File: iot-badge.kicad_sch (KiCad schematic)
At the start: 50 parts, among them J1 USB_C_Receptacle_USB2.0, J2 Wire ANT, Q1 BC847, Q2 BC847, SW1 SW_Push, SW2 SW_Push, SW3 SW_Push, SW4 SW_Push, SW5 SW_Push, SW6 SW_Push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

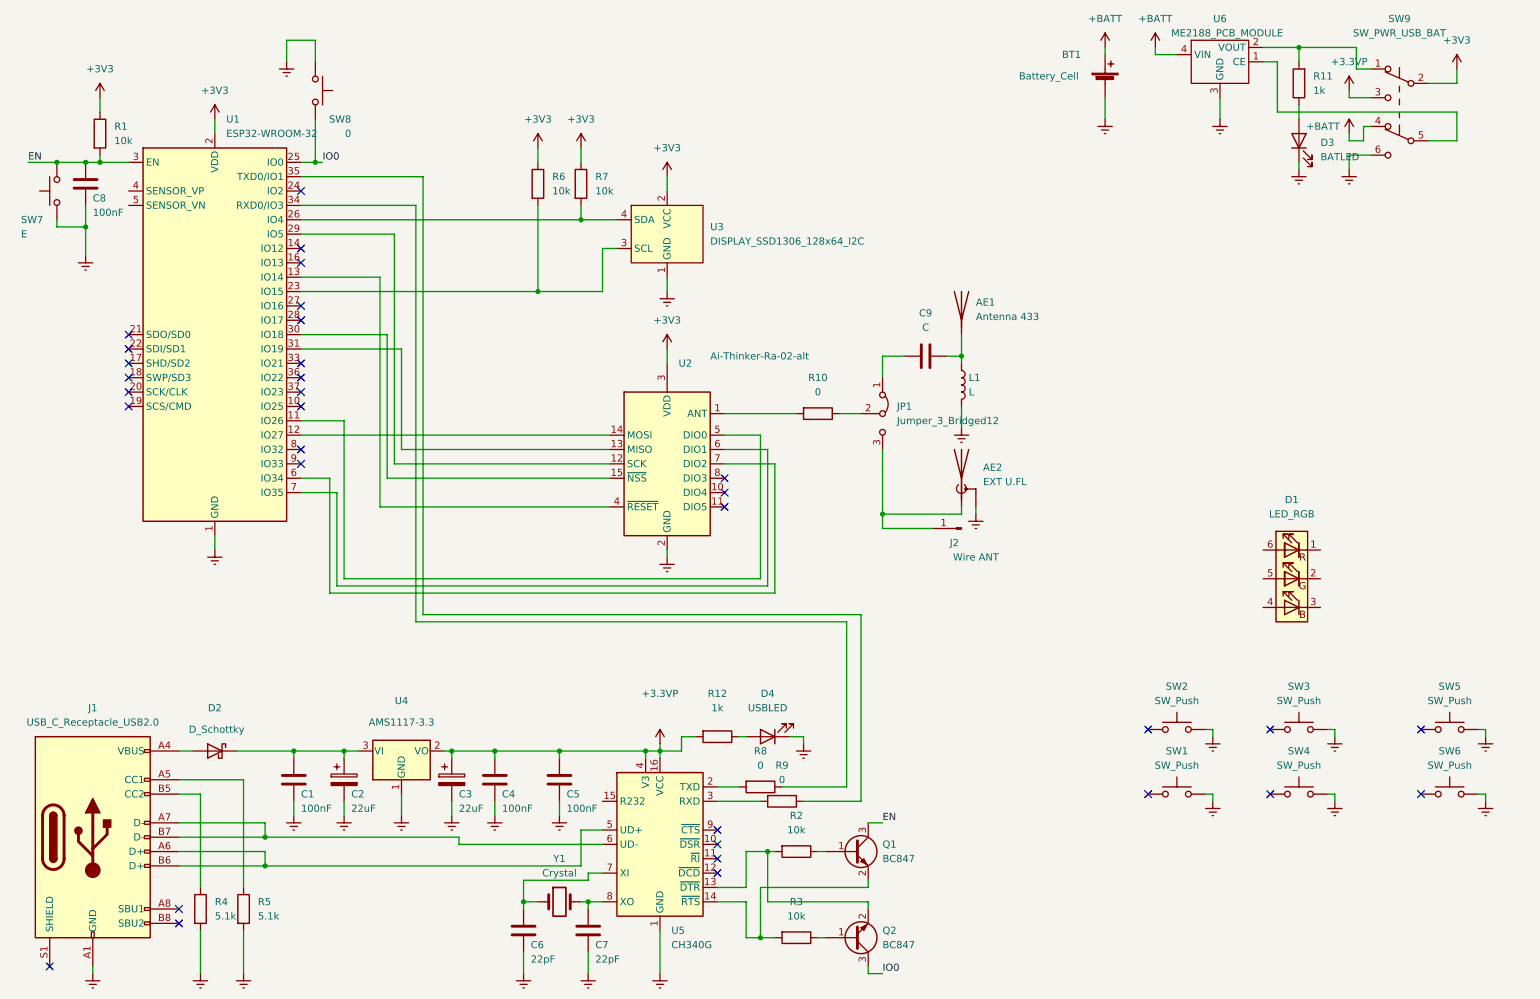
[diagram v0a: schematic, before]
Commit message: all elements placed and wired
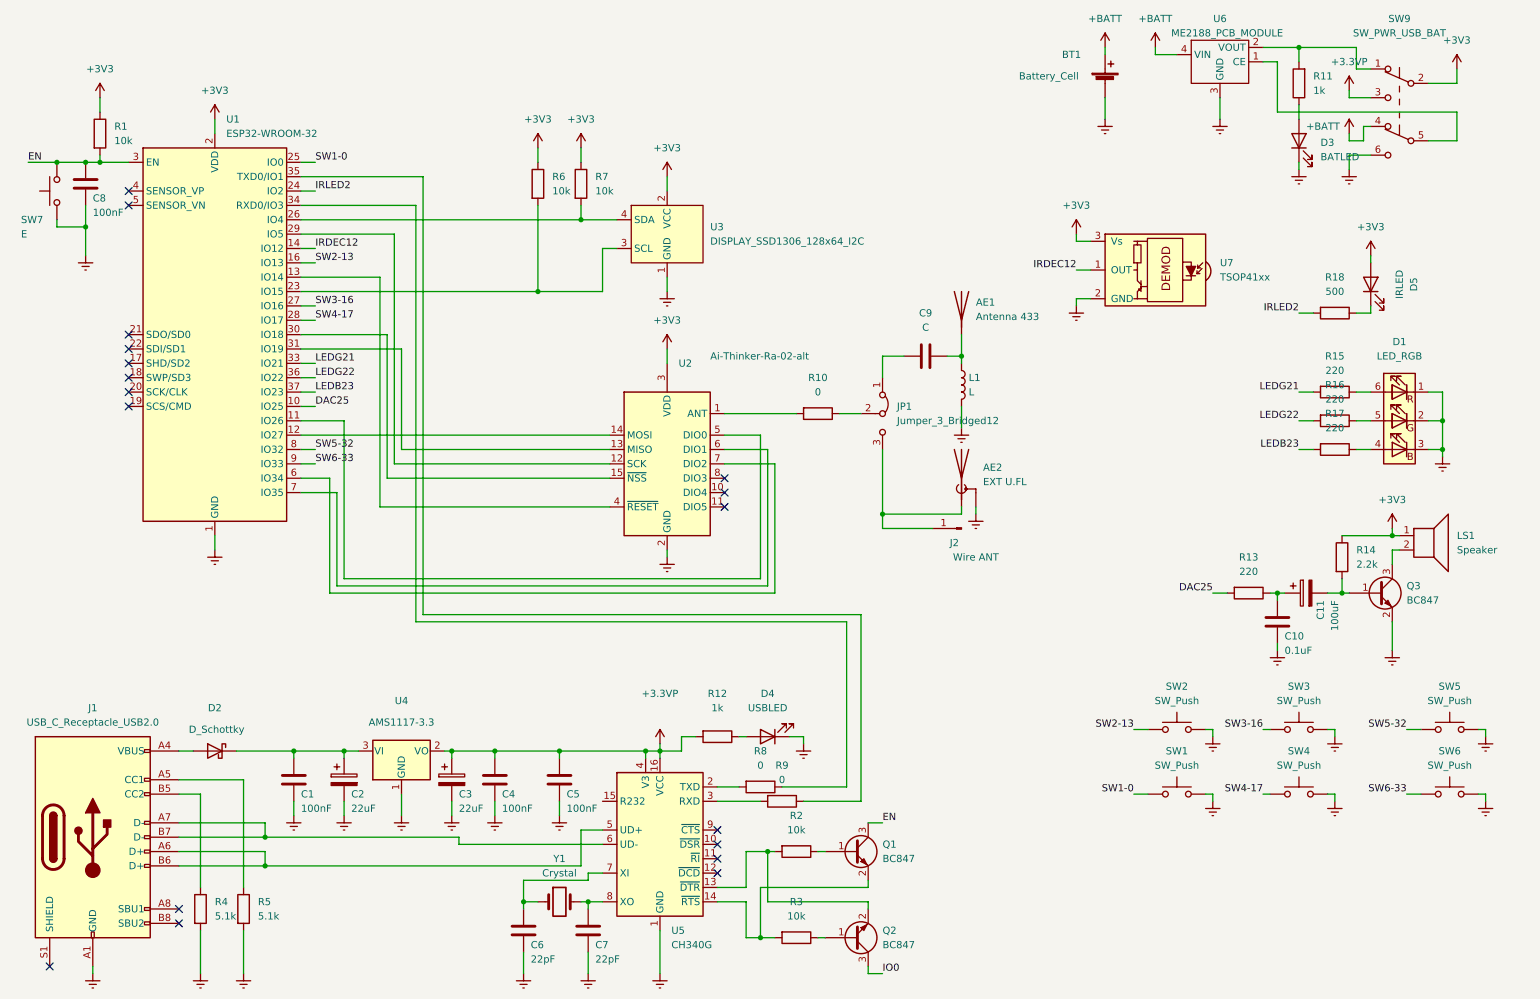
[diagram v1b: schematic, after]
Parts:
- removed SW8: 0, Button_Switch_SMD:SW_Push_SPST_NO_Alps_SKRK, symbol Switch:SW_Push
- added C10: 0.1uF, Capacitor_SMD:C_0805_2012Metric_Pad1.18x1.45mm_HandSolder, symbol Device:C
- added C11: 100uF, Capacitor_Tantalum_SMD:CP_EIA-2012-15_AVX-P_Pad1.30x1.05mm_HandSolder, symbol Device:C_Polarized
- added D5: IRLED, LED_SMD:LED_0805_2012Metric_Pad1.15x1.40mm_HandSolder, symbol Device:LED
- added LS1: Speaker, Speaker_SMD:Speaker_SMD-10mmx5mm, symbol Device:Speaker
- added Q3: BC847, Package_TO_SOT_SMD:SOT-23, symbol Transistor_BJT:BC847
- added R13, R15, R16, R17: 220, Resistor_SMD:R_0805_2012Metric_Pad1.20x1.40mm_HandSolder, symbol Device:R
- added R14: 2.2k, Resistor_SMD:R_0805_2012Metric_Pad1.20x1.40mm_HandSolder, symbol Device:R
- added R18: 500, Resistor_SMD:R_0805_2012Metric_Pad1.20x1.40mm_HandSolder, symbol Device:R
- added U7: TSOP41xx, OptoDevice:Vishay_MOLD-3Pin, symbol Interface_Optical:TSOP41xx
- BT1: footprint Battery:BatteryHolder_Keystone_2466_1xAAA -> Battery_SMD:BatteryHolder_Keystone_1020_1xAAA
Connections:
- net +3V3: now also D5.2 (A), LS1.1, R14.1, U7.3 (Vs)
- net Earth: now also D1.1 (RK), D1.2 (GK), D1.3 (BK), C10.2, Q3.2 (E), U7.2 (GND)
- net IO0: no longer U1.25 (IO0)
- net SW1-0: now reaches SW1.1
- net SW1-0: now also U1.25 (IO0)
- net SW5-32: now reaches SW5.1
- net SW5-32: now also U1.8 (IO32)
- net at D1.4 (BA): now also R17.1
- net at D1.5 (GA): now also R16.1
- net at D1.6 (RA): now also R15.1
- net SW6-33: now reaches SW6.1
- net SW6-33: now also U1.9 (IO33)
- net SW4-17: now reaches SW4.1
- net SW4-17: now also U1.28 (IO17)
- net SW3-16: now reaches SW3.1
- net SW3-16: now also U1.27 (IO16)
- net SW2-13: now reaches SW2.1
- net SW2-13: now also U1.16 (IO13)
- net DAC25: now reaches U1.10 (IO25)
- net DAC25: now also R13.2
- net IRDEC12: now reaches U1.14 (IO12)
- net IRDEC12: now also U7.1 (OUT)
- net IRLED2: now reaches U1.24 (IO2)
- net IRLED2: now also R18.2
- net LEDG21: now reaches U1.33 (IO21)
- net LEDG21: now also R15.2
- net LEDG22: now reaches U1.36 (IO22)
- net LEDG22: now also R16.2
- net LEDB23: now reaches U1.37 (IO23)
- net LEDB23: now also R17.2
- new net: C11.2, Q3.1 (B), R14.2
- new net: LS1.2, Q3.3 (C)
- new net: C10.1, C11.1, R13.1
- new net: D5.1 (K), R18.1
- no-connect marks 33 -> 18
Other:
- moved on the sheet: D1

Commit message: silk improvements
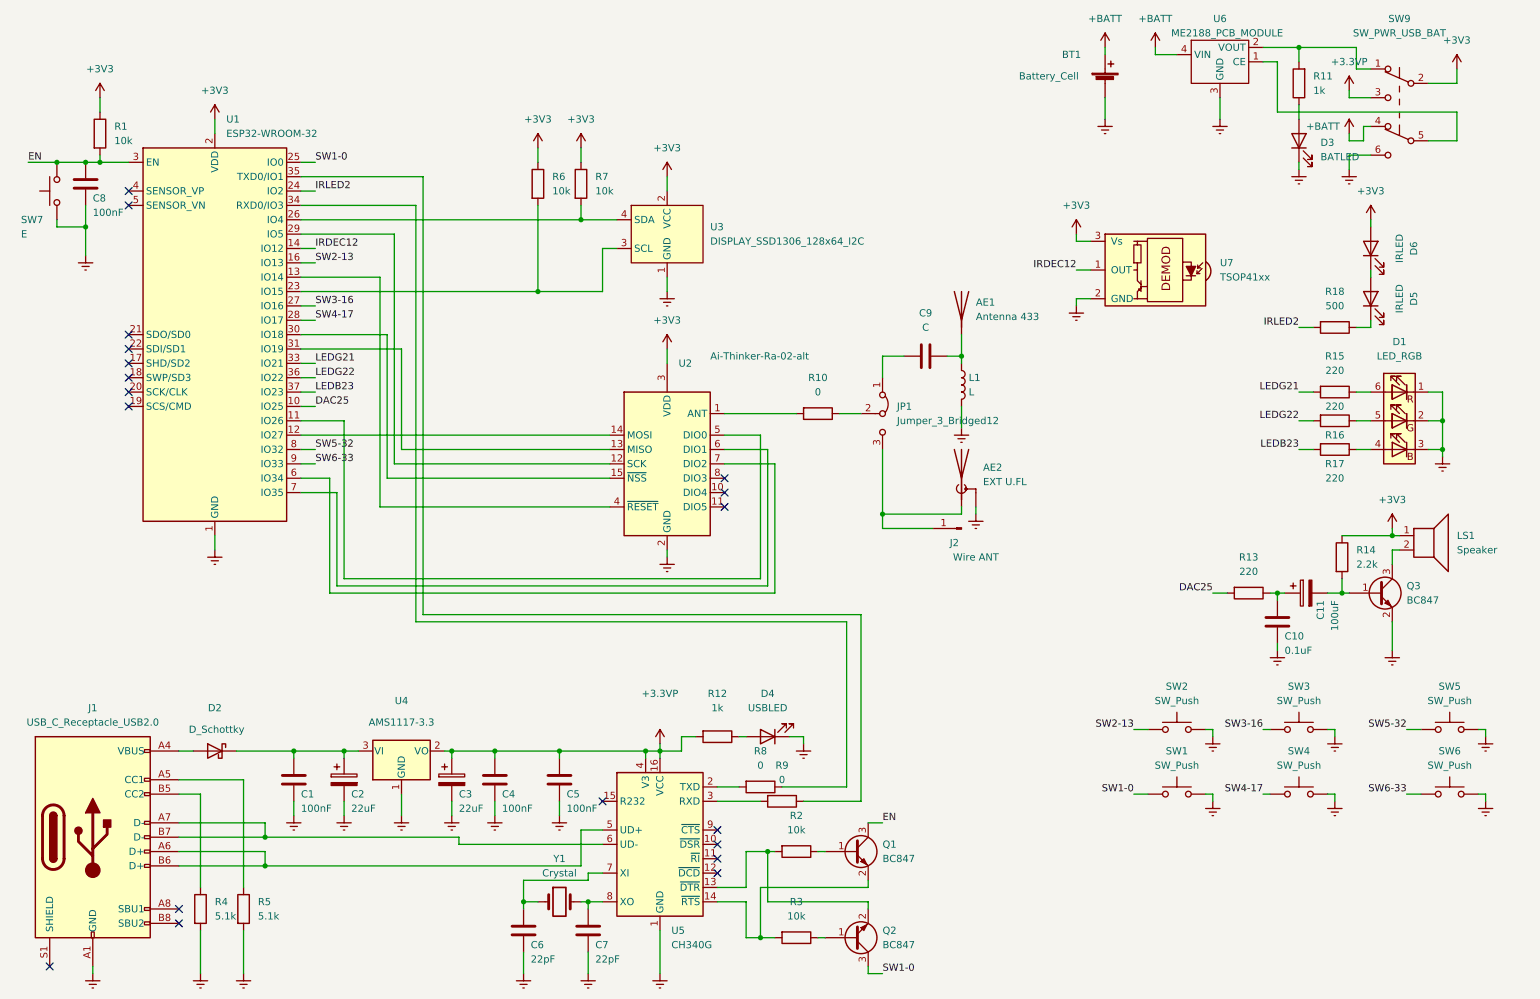
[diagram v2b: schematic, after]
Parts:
- added D6: IRLED, LED_SMD:LED_0805_2012Metric_Pad1.15x1.40mm_HandSolder, symbol Device:LED
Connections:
- net IO0 is gone; now on net SW1-0: Q2.3 (C)
- net +3V3: now also D6.2 (A); no longer D5.2 (A)
- new net: D5.2 (A), D6.1 (K)
- no-connect marks 18 -> 19
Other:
- moved on the sheet: D5, R18
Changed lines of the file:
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@@
   (no_connect (at 138.43 171.45))
   (no_connect (at 139.7 106.68))
+  (no_connect (at 118.11 158.75))
   (no_connect (at 34.29 50.8))
   (no_connect (at 20.32 187.96))
@@
     (stroke (width 0) (type default) (color 0 0 0 0))
   )
-  (wire (pts (xy 254 62.23) (xy 254 63.5))
-    (stroke (width 0) (type default) (color 0 0 0 0))
-  )
   (wire (pts (xy 92.71 166.37) (xy 92.71 165.1))
     (stroke (width 0) (type default) (color 0 0 0 0))
@@
     (stroke (width 0) (type default) (color 0 0 0 0))
   )
+  (wire (pts (xy 254 64.77) (xy 254 66.04))
+    (stroke (width 0) (type default) (color 0 0 0 0))
+  )
   (wire (pts (xy 138.43 158.75) (xy 146.05 158.75))
     (stroke (width 0) (type default) (color 0 0 0 0))
@@
     (stroke (width 0) (type default) (color 0 0 0 0))
   )
+  (wire (pts (xy 254 55.88) (xy 254 57.15))
+    (stroke (width 0) (type default) (color 0 0 0 0))
+  )
   (wire (pts (xy 128.27 149.86) (xy 128.27 151.13))
     (stroke (width 0) (type default) (color 0 0 0 0))
@@
     (stroke (width 0) (type default) (color 0 0 0 0))
   )
-  (wire (pts (xy 254 71.12) (xy 254 72.39))
+  (wire (pts (xy 254 73.66) (xy 254 74.93))
     (stroke (width 0) (type default) (color 0 0 0 0))
   )
@@
     (stroke (width 0) (type default) (color 0 0 0 0))
   )
-  (wire (pts (xy 251.46 72.39) (xy 254 72.39))
+  (wire (pts (xy 251.46 74.93) (xy 254 74.93))
     (stroke (width 0) (type default) (color 0 0 0 0))
   )
@@
     (stroke (width 0) (type default) (color 0 0 0 0))
   )
-  (wire (pts (xy 241.3 72.39) (xy 243.84 72.39))
+  (wire (pts (xy 241.3 74.93) (xy 243.84 74.93))
     (stroke (width 0) (type default) (color 0 0 0 0))
   )
@@
     (effects (font (size 1.27 1.27)) (justify left bottom))
   )
+  (label "SW1-0" (at 167.64 189.23 0)
+    (effects (font (size 1.27 1.27)) (justify left bottom))
+  )
   (label "LEDG22" (at 241.3 91.44 180)
     (effects (font (size 1.27 1.27)) (justify right bottom))
@@
     (effects (font (size 1.27 1.27)) (justify left bottom))
   )
-  (label "IO0" (at 167.64 189.23 0)
-    (effects (font (size 1.27 1.27)) (justify left bottom))
-  )
   (label "SW4-17" (at 234.95 157.48 180)
     (effects (font (size 1.27 1.27)) (justify right bottom))
@@
     (effects (font (size 1.27 1.27)) (justify left bottom))
   )
-  (label "IRLED2" (at 241.3 72.39 180)
+  (label "IRLED2" (at 241.3 74.93 180)
     (effects (font (size 1.27 1.27)) (justify right bottom))
   )
@@
   )
   (symbol (lib_id "Device:R") (at 247.65 96.52 270) (unit 1)
-    (in_bom yes) (on_board yes) (fields_autoplaced)
-    (property "Reference" "R17" (id 0) (at 247.65 90.17 90))
-    (property "Value" "220" (id 1) (at 247.65 92.71 90))
+    (in_bom yes) (on_board yes)
+    (property "Reference" "R17" (id 0) (at 247.65 99.06 90))
+    (property "Value" "220" (id 1) (at 247.65 101.6 90))
     (property "Footprint" "Resistor_SMD:R_0805_2012Metric_Pad1.20x1.40mm_HandSolder" (id 2) (at 247.65 94.742 90)
       (effects (font (size 1.27 1.27)) hide)
@@
     (pin "2")
   )
-  (symbol (lib_id "Device:LED") (at 254 67.31 90) (unit 1)
-    (in_bom yes) (on_board yes)
-    (property "Reference" "D5" (id 0) (at 261.62 67.31 0))
-    (property "Value" "IRLED" (id 1) (at 259.08 67.31 0))
-    (property "Footprint" "LED_SMD:LED_0805_2012Metric_Pad1.15x1.40mm_HandSolder" (id 2) (at 254 67.31 0)
-      (effects (font (size 1.27 1.27)) hide)
-    )
-    (property "Datasheet" "~" (id 3) (at 254 67.31 0)
+  (symbol (lib_id "Device:LED") (at 254 69.85 90) (unit 1)
+    (in_bom yes) (on_board yes)
+    (property "Reference" "D5" (id 0) (at 261.62 69.85 0))
+    (property "Value" "IRLED" (id 1) (at 259.08 69.85 0))
+    (property "Footprint" "LED_SMD:LED_0805_2012Metric_Pad1.15x1.40mm_HandSolder" (id 2) (at 254 69.85 0)
+      (effects (font (size 1.27 1.27)) hide)
+    )
+    (property "Datasheet" "~" (id 3) (at 254 69.85 0)
       (effects (font (size 1.27 1.27)) hide)
     )
@@
     (pin "2")
   )
-  (symbol (lib_id "power:+3V3") (at 254 62.23 0) (unit 1)
-    (in_bom yes) (on_board yes)
-    (property "Reference" "#PWR0137" (id 0) (at 254 66.04 0)
-      (effects (font (size 1.27 1.27)) hide)
-    )
-    (property "Value" "+3V3" (id 1) (at 254 57.15 0))
-    (property "Footprint" "" (id 2) (at 254 62.23 0)
-      (effects (font (size 1.27 1.27)) hide)
-    )
-    (property "Datasheet" "" (id 3) (at 254 62.23 0)
-      (effects (font (size 1.27 1.27)) hide)
-    )
-    (pin "1")
+  (symbol (lib_id "power:+3V3") (at 254 55.88 0) (unit 1)
+    (in_bom yes) (on_board yes)
+    (property "Reference" "#PWR0137" (id 0) (at 254 59.69 0)
+      (effects (font (size 1.27 1.27)) hide)
+    )
+    (property "Value" "+3V3" (id 1) (at 254 50.8 0))
+    (property "Footprint" "" (id 2) (at 254 55.88 0)
+      (effects (font (size 1.27 1.27)) hide)
+    )
+    (property "Datasheet" "" (id 3) (at 254 55.88 0)
+      (effects (font (size 1.27 1.27)) hide)
+    )
+    (pin "1")
+  )
+  (symbol (lib_id "Device:LED") (at 254 60.96 90) (unit 1)
+    (in_bom yes) (on_board yes)
+    (property "Reference" "D6" (id 0) (at 261.62 60.96 0))
+    (property "Value" "IRLED" (id 1) (at 259.08 60.96 0))
+    (property "Footprint" "LED_SMD:LED_0805_2012Metric_Pad1.15x1.40mm_HandSolder" (id 2) (at 254 60.96 0)
+      (effects (font (size 1.27 1.27)) hide)
+    )
+    (property "Datasheet" "~" (id 3) (at 254 60.96 0)
+      (effects (font (size 1.27 1.27)) hide)
+    )
+    (pin "1")
+    (pin "2")
   )
   (symbol (lib_id "power:Earth") (at 184.15 107.95 0) (unit 1)
@@
   )
   (symbol (lib_id "Device:R") (at 247.65 91.44 270) (unit 1)
-    (in_bom yes) (on_board yes) (fields_autoplaced)
-    (property "Reference" "R16" (id 0) (at 247.65 85.09 90))
-    (property "Value" "220" (id 1) (at 247.65 87.63 90))
+    (in_bom yes) (on_board yes)
+    (property "Reference" "R16" (id 0) (at 247.65 93.98 90))
+    (property "Value" "220" (id 1) (at 247.65 88.9 90))
     (property "Footprint" "Resistor_SMD:R_0805_2012Metric_Pad1.20x1.40mm_HandSolder" (id 2) (at 247.65 89.662 90)
       (effects (font (size 1.27 1.27)) hide)
@@
     (pin "3")
   )
-  (symbol (lib_id "Device:R") (at 247.65 72.39 270) (unit 1)
-    (in_bom yes) (on_board yes) (fields_autoplaced)
-    (property "Reference" "R18" (id 0) (at 247.65 66.04 90))
-    (property "Value" "500" (id 1) (at 247.65 68.58 90))
-    (property "Footprint" "Resistor_SMD:R_0805_2012Metric_Pad1.20x1.40mm_HandSolder" (id 2) (at 247.65 70.612 90)
-      (effects (font (size 1.27 1.27)) hide)
-    )
-    (property "Datasheet" "~" (id 3) (at 247.65 72.39 0)
+  (symbol (lib_id "Device:R") (at 247.65 74.93 270) (unit 1)
+    (in_bom yes) (on_board yes) (fields_autoplaced)
+    (property "Reference" "R18" (id 0) (at 247.65 68.58 90))
+    (property "Value" "500" (id 1) (at 247.65 71.12 90))
+    (property "Footprint" "Resistor_SMD:R_0805_2012Metric_Pad1.20x1.40mm_HandSolder" (id 2) (at 247.65 73.152 90)
+      (effects (font (size 1.27 1.27)) hide)
+    )
+    (property "Datasheet" "~" (id 3) (at 247.65 74.93 0)
       (effects (font (size 1.27 1.27)) hide)
     )
@@
       (reference "D5") (unit 1) (value "IRLED") (footprint "LED_SMD:LED_0805_2012Metric_Pad1.15x1.40mm_HandSolder")
     )
+    (path "/ad9affae-6bfc-4351-ab13-d56e9ad97c25"
+      (reference "D6") (unit 1) (value "IRLED") (footprint "LED_SMD:LED_0805_2012Metric_Pad1.15x1.40mm_HandSolder")
+    )
     (path "/b1b227c3-763e-438d-aed7-d3f1dd332c2c"

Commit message: all wired, unable to route
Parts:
- added R19, R20, R21, R22, R23, R24: 0, Resistor_SMD:R_0805_2012Metric_Pad1.20x1.40mm_HandSolder, symbol Device:R
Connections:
- net SW1-0: now also R22.2; no longer SW1.1
- net SW2-13: now also R21.2; no longer SW2.1
- net SW3-16: now also R23.2; no longer SW3.1
- net SW4-17: now also R24.2; no longer SW4.1
- net SW5-32: now also R19.2; no longer SW5.1
- net SW6-33: now also R20.2; no longer SW6.1
- net DAC25 renamed DAC-25
- net IRDEC12 renamed IRDEC-12
- net IRLED2 renamed IRLED-2
- net LEDB23 renamed LEDB-23
- net LEDG21 renamed LEDR-21
- net LEDG22 renamed LEDG-22
- new net: R22.1, SW1.1
- new net: R19.1, SW5.1
- new net: R20.1, SW6.1
- new net: R24.1, SW4.1
- new net: R21.1, SW2.1
- new net: R23.1, SW3.1
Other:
- moved on the sheet: SW1, SW2, SW3, SW4, SW5, SW6

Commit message: all wired, routed
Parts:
- removed R19, R20, R21, R22, R23, R24: 0, Resistor_SMD:R_0805_2012Metric_Pad1.20x1.40mm_HandSolder, symbol Device:R
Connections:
- net SW1-0: now also SW1.1
- net SW2-13: now also SW2.1
- net SW3-16: now also SW3.1
- net SW4-17: now also SW4.1
- net SW5-32: now also SW5.1
- net SW6-33: now also SW6.1
